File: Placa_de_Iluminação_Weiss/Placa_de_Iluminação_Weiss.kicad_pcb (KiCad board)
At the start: 2 copper layers, 52 x 19.9 mm, 8 parts

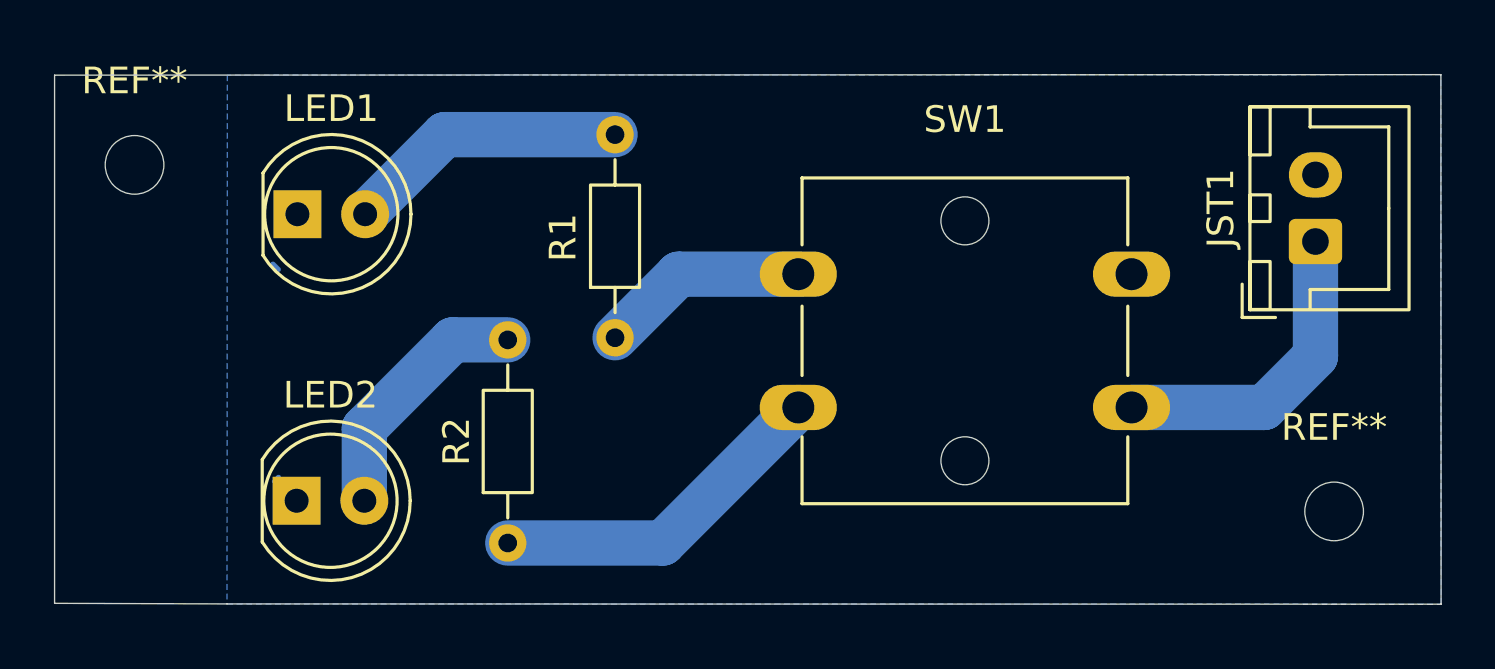
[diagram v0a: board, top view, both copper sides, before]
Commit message: feat: README da placa de processamento do foguete Weiss adicionado
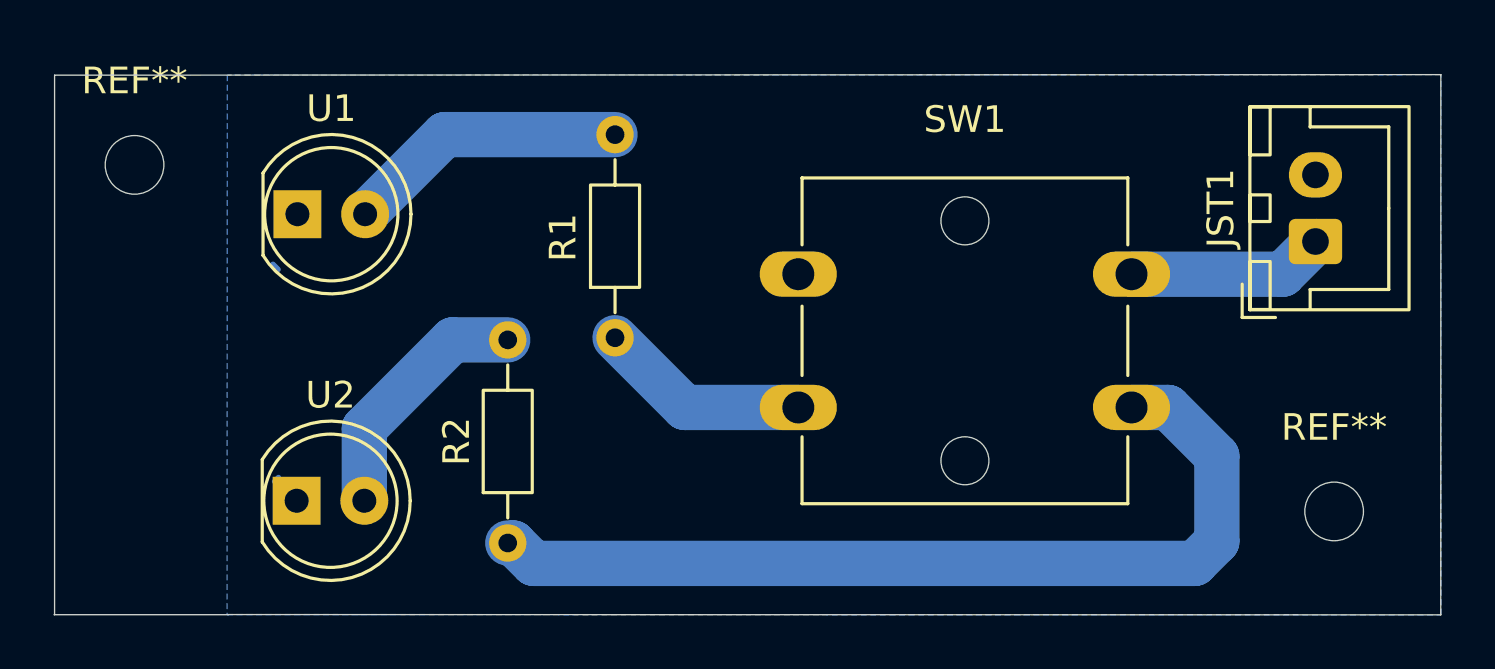
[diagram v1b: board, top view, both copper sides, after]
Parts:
- renumbered LED1 to U1, LED2 to U2
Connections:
- R2 pad 1: Net-(R2-Pad1) -> Net-(SW1-K)
- SW1 pad 1: Net-(R1-Pad1) -> unconnected-(SW1-Pad1)
- SW1 pad 2: Net-(R2-Pad1) -> Net-(R1-Pad1)
- SW1 pad 3: +3.3V -> Net-(SW1-K)
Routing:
- net Net-(SW1-K): track 0.00 -> 34.9 mm
- net Net-(R2-Pad1): track 13.0 -> 0.00 mm
- net +3.3V: track 12.0 -> 7.41 mm
- net unconnected-(SW1-Pad1): track 0.00 -> 0.70 mm
- net Net-(R1-Pad1): track 8.57 -> 7.96 mm
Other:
- board size 52 x 19.9 mm -> 52 x 20.3 mm
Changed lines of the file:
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@@
 			(layers "*.Cu" "*.Mask")
 			(remove_unused_layers no)
-			(net "Net-(R1-Pad1)")
+			(net "unconnected-(SW1-Pad1)")
 			(pinfunction "1_1")
 			(pintype "passive")
@@
 			(layers "*.Cu" "*.Mask")
 			(remove_unused_layers no)
-			(net "Net-(R2-Pad1)")
+			(net "Net-(R1-Pad1)")
 			(pinfunction "2_2")
 			(pintype "passive")
@@
 			(layers "*.Cu" "*.Mask")
 			(remove_unused_layers no)
-			(net "+3.3V")
+			(net "Net-(SW1-K)")
 			(pinfunction "K_3")
 			(pintype "passive")
@@
 		(descr "LED, diameter 5.0mm, 2 pins, http://cdn-reichelt.de/documents/datenblatt/A500/LL-504BC2E-009.pdf, generated by kicad-footprint-generator")
 		(tags "LED")
-		(property "Reference" "LED2"
+		(property "Reference" "U2"
 			(at 1.27 -3.96 0)
 			(layer "F.SilkS")
@@
 		)
 		(property "Value" "MountingHole_2.2mm_M2"
-			(at 0 3.15 0)
+			(at -5.375 4.625 0)
 			(layer "F.Fab")
 			(effects
@@
 			(layers "*.Cu" "*.Mask")
 			(remove_unused_layers no)
-			(net "Net-(R2-Pad1)")
+			(net "Net-(SW1-K)")
 			(pintype "passive")
 		)
@@
 		(descr "LED, diameter 5.0mm, 2 pins, http://cdn-reichelt.de/documents/datenblatt/A500/LL-504BC2E-009.pdf, generated by kicad-footprint-generator")
 		(tags "LED")
-		(property "Reference" "LED1"
+		(property "Reference" "U1"
 			(at 1.27 -3.96 0)
 			(layer "F.SilkS")
@@
 	)
 	(gr_line
-		(start 108 68.63433)
-		(end 108 88.447805)
+		(start 107.977813 88.875)
+		(end 114.522186 88.875)
 		(stroke
 			(width 0.05)
@@
 	)
 	(gr_line
-		(start 108 88.447805)
-		(end 114.469992 88.469607)
+		(start 108.000707 68.636766)
+		(end 108.000052 88.875)
 		(stroke
 			(width 0.05)
@@
 	)
 	(gr_line
-		(start 114.469992 88.469607)
-		(end 160.013201 88.48087)
+		(start 114.495942 88.869379)
+		(end 160 88.880621)
 		(stroke
 			(width 0.05)
@@
 	)
 	(gr_line
+		(start 160 88.880621)
+		(end 160.004697 68.614842)
+		(stroke
+			(width 0.05)
+			(type default)
+		)
+		(layer "Edge.Cuts")
+	)
+	(gr_line
 		(start 160.004697 68.614842)
 		(end 108 68.63433)
@@
 		(layer "Edge.Cuts")
 	)
-	(gr_line
-		(start 160.013201 88.48087)
-		(end 160.004697 68.614842)
-		(stroke
-			(width 0.05)
-			(type default)
-		)
-		(layer "Edge.Cuts")
+	(segment
+		(start 148.4 76.1)
+		(end 154.075 76.1)
+		(width 1.7)
+		(layer "B.Cu")
+		(net "+3.3V")
+	)
+	(segment
+		(start 154.075 76.1)
+		(end 155.3 74.875)
+		(width 1.7)
+		(layer "B.Cu")
+		(net "+3.3V")
+	)
+	(segment
+		(start 122.935 78.565)
+		(end 119.62 81.88)
+		(width 1.7)
+		(layer "B.Cu")
+		(net "Net-(R2-Pad2)")
+	)
+	(segment
+		(start 119.62 81.88)
+		(end 119.62 84.6)
+		(width 1.7)
+		(layer "B.Cu")
+		(net "Net-(R2-Pad2)")
+	)
+	(segment
+		(start 125 78.565)
+		(end 122.935 78.565)
+		(width 1.7)
+		(layer "B.Cu")
+		(net "Net-(R2-Pad2)")
+	)
+	(segment
+		(start 116.39 75.925)
+		(end 116.19 75.725)
+		(width 0.2)
+		(layer "B.Cu")
+		(net "GND")
+	)
+	(segment
+		(start 116.4 83.725)
+		(end 116.25 83.875)
+		(width 0.2)
+		(layer "B.Cu")
+		(net "GND")
+	)
+	(segment
+		(start 129.025 70.865)
+		(end 122.635 70.865)
+		(width 1.7)
+		(layer "B.Cu")
+		(net "Net-(R1-Pad2)")
+	)
+	(segment
+		(start 122.635 70.865)
+		(end 119.65 73.85)
+		(width 1.7)
+		(layer "B.Cu")
+		(net "Net-(R1-Pad2)")
+	)
+	(segment
+		(start 125.31 86.185)
+		(end 125.425 86.3)
+		(width 0.2)
+		(layer "F.Cu")
+		(net "Net-(SW1-K)")
+	)
+	(segment
+		(start 125 86.185)
+		(end 125.31 86.185)
+		(width 0.2)
+		(layer "F.Cu")
+		(net "Net-(SW1-K)")
+	)
+	(segment
+		(start 151.6 86.125)
+		(end 151.6 82.925)
+		(width 1.7)
+		(layer "B.Cu")
+		(net "Net-(SW1-K)")
+	)
+	(segment
+		(start 151.6 82.925)
+		(end 149.775 81.1)
+		(width 1.7)
+		(layer "B.Cu")
+		(net "Net-(SW1-K)")
+	)
+	(segment
+		(start 125.207323 86.185)
+		(end 125.972323 86.95)
+		(width 1.7)
+		(layer "B.Cu")
+		(net "Net-(SW1-K)")
+	)
+	(segment
+		(start 150.775 86.95)
+		(end 151.6 86.125)
+		(width 1.7)
+		(layer "B.Cu")
+		(net "Net-(SW1-K)")
+	)
+	(segment
+		(start 149.775 81.1)
+		(end 148.4 81.1)
+		(width 1.7)
+		(layer "B.Cu")
+		(net "Net-(SW1-K)")
+	)
+	(segment
+		(start 125 86.185)
+		(end 125.207323 86.185)
+		(width 1.7)
+		(layer "B.Cu")
+		(net "Net-(SW1-K)")
+	)
+	(segment
+		(start 125.972323 86.95)
+		(end 150.775 86.95)
+		(width 1.7)
+		(layer "B.Cu")
+		(net "Net-(SW1-K)")
 	)
 	(segment
@@
 		(width 0.2)
 		(layer "B.Cu")
-		(net "Net-(R1-Pad1)")
-	)
-	(segment
-		(start 131.41 76.1)
-		(end 129.025 78.485)
-		(width 1.7)
-		(layer "B.Cu")
-		(net "Net-(R1-Pad1)")
+		(net "unconnected-(SW1-Pad1)")
 	)
 	(segment
@@
 		(width 0.2)
 		(layer "B.Cu")
+		(net "unconnected-(SW1-Pad1)")
+	)
+	(segment
+		(start 129.025 78.485)
+		(end 131.64 81.1)
+		(width 1.7)
+		(layer "B.Cu")
 		(net "Net-(R1-Pad1)")
 	)
 	(segment
-		(start 135.9 76.1)
-		(end 131.41 76.1)
+		(start 131.64 81.1)
+		(end 135.9 81.1)
 		(width 1.7)
 		(layer "B.Cu")
 		(net "Net-(R1-Pad1)")
-	)
-	(segment
-		(start 130.815 86.185)
-		(end 135.9 81.1)
-		(width 1.7)
-		(layer "B.Cu")
-		(net "Net-(R2-Pad1)")
-	)
-	(segment
-		(start 125 86.185)
-		(end 130.815 86.185)
-		(width 1.7)
-		(layer "B.Cu")
-		(net "Net-(R2-Pad1)")
-	)
-	(segment
-		(start 148.4 81.1)
-		(end 153.375 81.1)
-		(width 1.7)
-		(layer "B.Cu")
-		(net "+3.3V")
-	)
-	(segment
-		(start 155.3 79.175)
-		(end 155.3 74.875)
-		(width 1.7)
-		(layer "B.Cu")
-		(net "+3.3V")
-	)
-	(segment
-		(start 153.375 81.1)
-		(end 155.3 79.175)
-		(width 1.7)
-		(layer "B.Cu")
-		(net "+3.3V")
-	)
-	(segment
-		(start 122.935 78.565)
-		(end 119.62 81.88)
-		(width 1.7)
-		(layer "B.Cu")
-		(net "Net-(R2-Pad2)")
-	)
-	(segment
-		(start 119.62 81.88)
-		(end 119.62 84.6)
-		(width 1.7)
-		(layer "B.Cu")
-		(net "Net-(R2-Pad2)")
-	)
-	(segment
-		(start 125 78.565)
-		(end 122.935 78.565)
-		(width 1.7)
-		(layer "B.Cu")
-		(net "Net-(R2-Pad2)")
-	)
-	(segment
-		(start 116.39 75.925)
-		(end 116.19 75.725)
-		(width 0.2)
-		(layer "B.Cu")
-		(net "GND")
-	)
-	(segment
-		(start 116.4 83.725)
-		(end 116.25 83.875)
-		(width 0.2)
-		(layer "B.Cu")
-		(net "GND")
-	)
-	(segment
-		(start 129.025 70.865)
-		(end 122.635 70.865)
-		(width 1.7)
-		(layer "B.Cu")
-		(net "Net-(R1-Pad2)")
-	)
-	(segment
-		(start 122.635 70.865)
-		(end 119.65 73.85)
-		(width 1.7)
-		(layer "B.Cu")
-		(net "Net-(R1-Pad2)")
 	)
 	(zone
@@
 		(polygon
 			(pts
-				(xy 114.480005 68.63433) (xy 114.469992 88.469607) (xy 160.013201 88.48087) (xy 160.004697 68.614842)
-			)
-		)
+				(xy 114.480005 68.63433) (xy 114.469789 88.869366) (xy 160.013371 88.88063) (xy 160.004697 68.614842)
+			)
+		)
